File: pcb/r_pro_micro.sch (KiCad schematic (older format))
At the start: 27 parts, among them J1 Conn_01x12, J2 USB_A, J3 Conn_01x12, U1 MIC5219-2.5YM5, U2 ATmega32U4-MU, Y1 16MHz

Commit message: ** Se agregan footprints **
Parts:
- C1, C2: footprint (none) -> Capacitor_Tantalum_SMD:CP_EIA-3216-10_Kemet-I
- C3, C4, C5, C6, C7, C8, C9: footprint (none) -> Capacitor_SMD:C_0201_0603Metric
- D1: footprint (none) -> Diode_SMD:D_SOD-323
- D2, D3, D4: footprint (none) -> LED_SMD:LED_0201_0603Metric
- F1: footprint (none) -> Fuse:Fuse_1206_3216Metric
- J1, J3: footprint (none) -> Connector_PinHeader_2.54mm:PinHeader_1x12_P2.54mm_Vertical
- J2: footprint (none) -> Connector_USB:USB_Micro-AB_Molex_47590-0001; symbol Connector:USB_A -> r_pro_micro-rescue:USB_A-Connector
- R1, R2, R3, R4, R5, R6, R7: footprint (none) -> Resistor_SMD:R_0603_1608Metric
- Y1: footprint (none) -> Crystal:Crystal_SMD_5032-4Pin_5.0x3.2mm
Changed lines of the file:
@@
 F 0 "C6" H 7200 3050 50  0000 C CNN
 F 1 "22pF" H 7250 2850 50  0000 C CNN
-F 2 "" H 7150 2950 50  0001 C CNN
+F 2 "Capacitor_SMD:C_0201_0603Metric" H 7150 2950 50  0001 C CNN
 F 3 "~" H 7150 2950 50  0001 C CNN
 	1    7150 2950
@@
 F 0 "C5" H 7500 3050 50  0000 C CNN
 F 1 "22pF" H 7500 2850 50  0000 C CNN
-F 2 "" H 7600 2950 50  0001 C CNN
+F 2 "Capacitor_SMD:C_0201_0603Metric" H 7600 2950 50  0001 C CNN
 F 3 "~" H 7600 2950 50  0001 C CNN
 	1    7600 2950
@@
 F 0 "Y1" H 7350 2400 50  0000 L CNN
 F 1 "16MHz" H 7300 2600 50  0000 L CNN
-F 2 "" H 7400 2500 50  0001 C CNN
+F 2 "Crystal:Crystal_SMD_5032-4Pin_5.0x3.2mm" H 7400 2500 50  0001 C CNN
 F 3 "~" H 7400 2500 50  0001 C CNN
 	1    7400 2500
@@
 F 0 "R4" H 8100 1950 50  0000 L CNN
 F 1 "10K" H 8050 1850 50  0000 L CNN
-F 2 "" H 8250 1900 50  0001 C CNN
+F 2 "Resistor_SMD:R_0603_1608Metric" H 8250 1900 50  0001 C CNN
 F 3 "~" H 8250 1900 50  0001 C CNN
 	1    8250 1900
@@
 F 0 "C7" V 8200 2600 50  0000 C CNN
 F 1 "0.1uF" V 8300 2550 50  0000 C CNN
-F 2 "" H 8250 2700 50  0001 C CNN
+F 2 "Capacitor_SMD:C_0201_0603Metric" H 8250 2700 50  0001 C CNN
 F 3 "~" H 8250 2700 50  0001 C CNN
 	1    8250 2700
@@
 F 0 "C8" V 8150 3300 50  0000 C CNN
 F 1 "1uF" V 8250 3250 50  0000 C CNN
-F 2 "" H 8200 3400 50  0001 C CNN
+F 2 "Capacitor_SMD:C_0201_0603Metric" H 8200 3400 50  0001 C CNN
 F 3 "~" H 8200 3400 50  0001 C CNN
 	1    8200 3400
@@
 F 0 "D4" V 10654 3148 50  0000 L CNN
 F 1 "Green" V 10745 3148 50  0000 L CNN
-F 2 "" V 10700 3050 50  0001 C CNN
+F 2 "LED_SMD:LED_0201_0603Metric" V 10700 3050 50  0001 C CNN
 F 3 "~" V 10700 3050 50  0001 C CNN
 	1    10700 3050
@@
 F 0 "R6" H 10759 3596 50  0000 L CNN
 F 1 "330" H 10759 3505 50  0000 L CNN
-F 2 "" H 10700 3550 50  0001 C CNN
+F 2 "Resistor_SMD:R_0603_1608Metric" H 10700 3550 50  0001 C CNN
 F 3 "~" H 10700 3550 50  0001 C CNN
 	1    10700 3550
@@
 F 0 "R5" H 10759 1796 50  0000 L CNN
 F 1 "330" H 10759 1705 50  0000 L CNN
-F 2 "" H 10700 1750 50  0001 C CNN
+F 2 "Resistor_SMD:R_0603_1608Metric" H 10700 1750 50  0001 C CNN
 F 3 "~" H 10700 1750 50  0001 C CNN
 	1    10700 1750
@@
 F 0 "D3" V 10654 1398 50  0000 L CNN
 F 1 "Yellow" V 10745 1398 50  0000 L CNN
-F 2 "" V 10700 1300 50  0001 C CNN
+F 2 "LED_SMD:LED_0201_0603Metric" V 10700 1300 50  0001 C CNN
 F 3 "~" V 10700 1300 50  0001 C CNN
 	1    10700 1300
@@
 Wire Notes Line
 	7000 500  7000 6150
-Text Notes 9800 950  2    100  ~ 0
+Text Notes 9800 950  2    100  ~ 20
 MICROCONTROLADOR
 $Comp
@@
 F 0 "J3" H 6450 2550 50  0000 L CNN
 F 1 "Conn_01x12" H 6300 2450 50  0000 L CNN
-F 2 "" H 6500 1800 50  0001 C CNN
+F 2 "Connector_PinHeader_2.54mm:PinHeader_1x12_P2.54mm_Vertical" H 6500 1800 50  0001 C CNN
 F 3 "~" H 6500 1800 50  0001 C CNN
 	1    6500 1800
@@
 Wire Wire Line
 	6300 2400 6050 2400
-Text Notes 5200 800  0    100  ~ 0
+Text Notes 5200 800  0    100  ~ 20
 PIN HEADERS
 Wire Notes Line
@@
 NoConn ~ 9600 4600
 $Comp
-L Connector:USB_A J2
+L r_pro_micro-rescue:USB_A-Connector J2
 U 1 1 5F660175
 P 5150 4400
 F 0 "J2" H 5207 4867 50  0000 C CNN
 F 1 "USB_A" H 5207 4776 50  0000 C CNN
-F 2 "" H 5300 4350 50  0001 C CNN
+F 2 "Connector_USB:USB_Micro-AB_Molex_47590-0001" H 5300 4350 50  0001 C CNN
 F 3 " ~" H 5300 4350 50  0001 C CNN
 	1    5150 4400
@@
 F 0 "R2" V 5650 4300 50  0000 C CNN
 F 1 "22" V 5650 4500 50  0000 C CNN
-F 2 "" H 5750 4400 50  0001 C CNN
+F 2 "Resistor_SMD:R_0603_1608Metric" H 5750 4400 50  0001 C CNN
 F 3 "~" H 5750 4400 50  0001 C CNN
 	1    5750 4400
@@
 F 0 "R3" V 5850 4400 50  0000 C CNN
 F 1 "22" V 5850 4600 50  0000 C CNN
-F 2 "" H 5750 4500 50  0001 C CNN
+F 2 "Resistor_SMD:R_0603_1608Metric" H 5750 4500 50  0001 C CNN
 F 3 "~" H 5750 4500 50  0001 C CNN
 	1    5750 4500
@@
 Wire Notes Line
 	4350 6150 11200 6150
-Text Notes 5500 3250 0    100  ~ 0
+Text Notes 5500 3250 0    100  ~ 20
 USB
 Wire Notes Line
@@
 F 0 "J1" H 4718 1075 50  0000 C CNN
 F 1 "Conn_01x12" H 4718 1166 50  0000 C CNN
-F 2 "" H 4800 1900 50  0001 C CNN
+F 2 "Connector_PinHeader_2.54mm:PinHeader_1x12_P2.54mm_Vertical" H 4800 1900 50  0001 C CNN
 F 3 "~" H 4800 1900 50  0001 C CNN
 	1    4800 1900
@@
 F 0 "C1" H 1741 2646 50  0000 L CNN
 F 1 "10uF" H 1741 2555 50  0000 L CNN
-F 2 "" H 1650 2600 50  0001 C CNN
+F 2 "Capacitor_Tantalum_SMD:CP_EIA-3216-10_Kemet-I" H 1650 2600 50  0001 C CNN
 F 3 "~" H 1650 2600 50  0001 C CNN
 	1    1650 2600
@@
 F 0 "C2" H 2991 2646 50  0000 L CNN
 F 1 "10uF" H 2991 2555 50  0000 L CNN
-F 2 "" H 2900 2600 50  0001 C CNN
+F 2 "Capacitor_Tantalum_SMD:CP_EIA-3216-10_Kemet-I" H 2900 2600 50  0001 C CNN
 F 3 "~" H 2900 2600 50  0001 C CNN
 	1    2900 2600
@@
 F 0 "C3" H 3400 2700 50  0000 C CNN
 F 1 "1uF" H 3400 2500 50  0000 C CNN
-F 2 "" H 3300 2600 50  0001 C CNN
+F 2 "Capacitor_SMD:C_0201_0603Metric" H 3300 2600 50  0001 C CNN
 F 3 "~" H 3300 2600 50  0001 C CNN
 	1    3300 2600
@@
 F 0 "C4" H 3700 2700 50  0000 C CNN
 F 1 "1uF" H 3700 2500 50  0000 C CNN
-F 2 "" H 3600 2600 50  0001 C CNN
+F 2 "Capacitor_SMD:C_0201_0603Metric" H 3600 2600 50  0001 C CNN
 F 3 "~" H 3600 2600 50  0001 C CNN
 	1    3600 2600
@@
 F 0 "R1" H 4009 2696 50  0000 L CNN
 F 1 "1K" H 4009 2605 50  0000 L CNN
-F 2 "" H 3950 2650 50  0001 C CNN
+F 2 "Resistor_SMD:R_0603_1608Metric" H 3950 2650 50  0001 C CNN
 F 3 "~" H 3950 2650 50  0001 C CNN
 	1    3950 2650
@@
 F 0 "D2" V 3900 3000 50  0000 L CNN
 F 1 "Red" V 4000 2900 50  0000 L CNN
-F 2 "" V 3950 3200 50  0001 C CNN
+F 2 "LED_SMD:LED_0201_0603Metric" V 3950 3200 50  0001 C CNN
 F 3 "~" V 3950 3200 50  0001 C CNN
 	1    3950 3200
@@
 F 0 "F1" V 795 2000 50  0000 C CNN
 F 1 "500mA" V 886 2000 50  0000 C CNN
-F 2 "" H 1050 1800 50  0001 L CNN
+F 2 "Fuse:Fuse_1206_3216Metric" H 1050 1800 50  0001 L CNN
 F 3 "~" H 1000 2000 50  0001 C CNN
 	1    1000 2000
@@
 F 0 "D1" H 1450 1793 50  0000 C CNN
 F 1 "D" H 1450 1884 50  0000 C CNN
-F 2 "" V 1450 2000 50  0001 C CNN
+F 2 "Diode_SMD:D_SOD-323" V 1450 2000 50  0001 C CNN
 F 3 "~" V 1450 2000 50  0001 C CNN
 	1    1450 2000
@@
 Wire Wire Line
 	1650 2000 1650 2350
-Text Notes 2000 1450 0    100  ~ 0
+Text Notes 2000 1450 0    100  ~ 20
 REGULADOR
 Wire Wire Line
@@
 F 0 "C9" H 2300 4250 50  0000 C CNN
 F 1 "1uF" H 2300 4050 50  0000 C CNN
-F 2 "" H 2200 4150 50  0001 C CNN
+F 2 "Capacitor_SMD:C_0201_0603Metric" H 2200 4150 50  0001 C CNN
 F 3 "~" H 2200 4150 50  0001 C CNN
 	1    2200 4150
@@
 F 0 "R7" V 10200 4150 50  0000 L CNN
 F 1 "0" V 10400 4150 50  0000 L CNN
-F 2 "" H 10300 4200 50  0001 C CNN
+F 2 "Resistor_SMD:R_0603_1608Metric" H 10300 4200 50  0001 C CNN
 F 3 "~" H 10300 4200 50  0001 C CNN
 	1    10300 4200

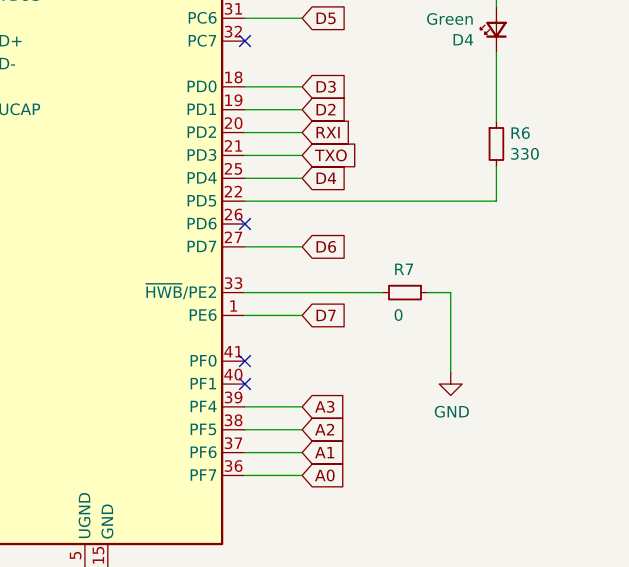
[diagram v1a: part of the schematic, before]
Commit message: ** Se crea netlist cambiando R 0omhs por nettie **
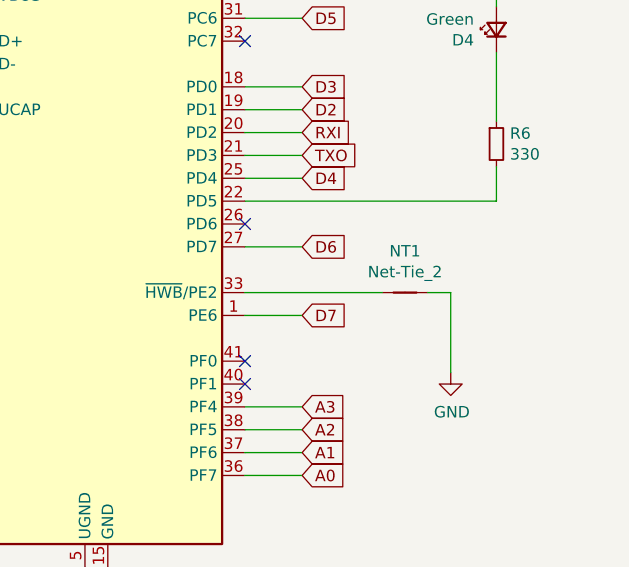
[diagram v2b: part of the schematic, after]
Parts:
- removed R7: 0, Resistor_SMD:R_0603_1608Metric, symbol Device:R_Small
- added NT1: Net-Tie_2, NetTie:NetTie-2_SMD_Pad0.5mm, symbol Device:Net-Tie_2
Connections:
- net GND: now also NT1.2
- net at U2.33 (~HWB~/PE2): now also NT1.1
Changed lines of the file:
@@
 Wire Wire Line
 	1650 2800 1650 2850
-$Comp
-L Device:R_Small R7
-U 1 1 5F6CBCA3
-P 10300 4200
-F 0 "R7" V 10200 4150 50  0000 L CNN
-F 1 "0" V 10400 4150 50  0000 L CNN
-F 2 "Resistor_SMD:R_0603_1608Metric" H 10300 4200 50  0001 C CNN
-F 3 "~" H 10300 4200 50  0001 C CNN
-	1    10300 4200
-	0    1    1    0
-$EndComp
 Wire Wire Line
 	10200 4200 9600 4200
@@
 	1    0    0    -1
 $EndComp
+$Comp
+L Device:Net-Tie_2 NT1
+U 1 1 5F7FD2D5
+P 10300 4200
+F 0 "NT1" H 10300 4381 50  0000 C CNN
+F 1 "Net-Tie_2" H 10300 4290 50  0000 C CNN
+F 2 "NetTie:NetTie-2_SMD_Pad0.5mm" H 10300 4200 50  0001 C CNN
+F 3 "~" H 10300 4200 50  0001 C CNN
+	1    10300 4200
+	1    0    0    -1
+$EndComp

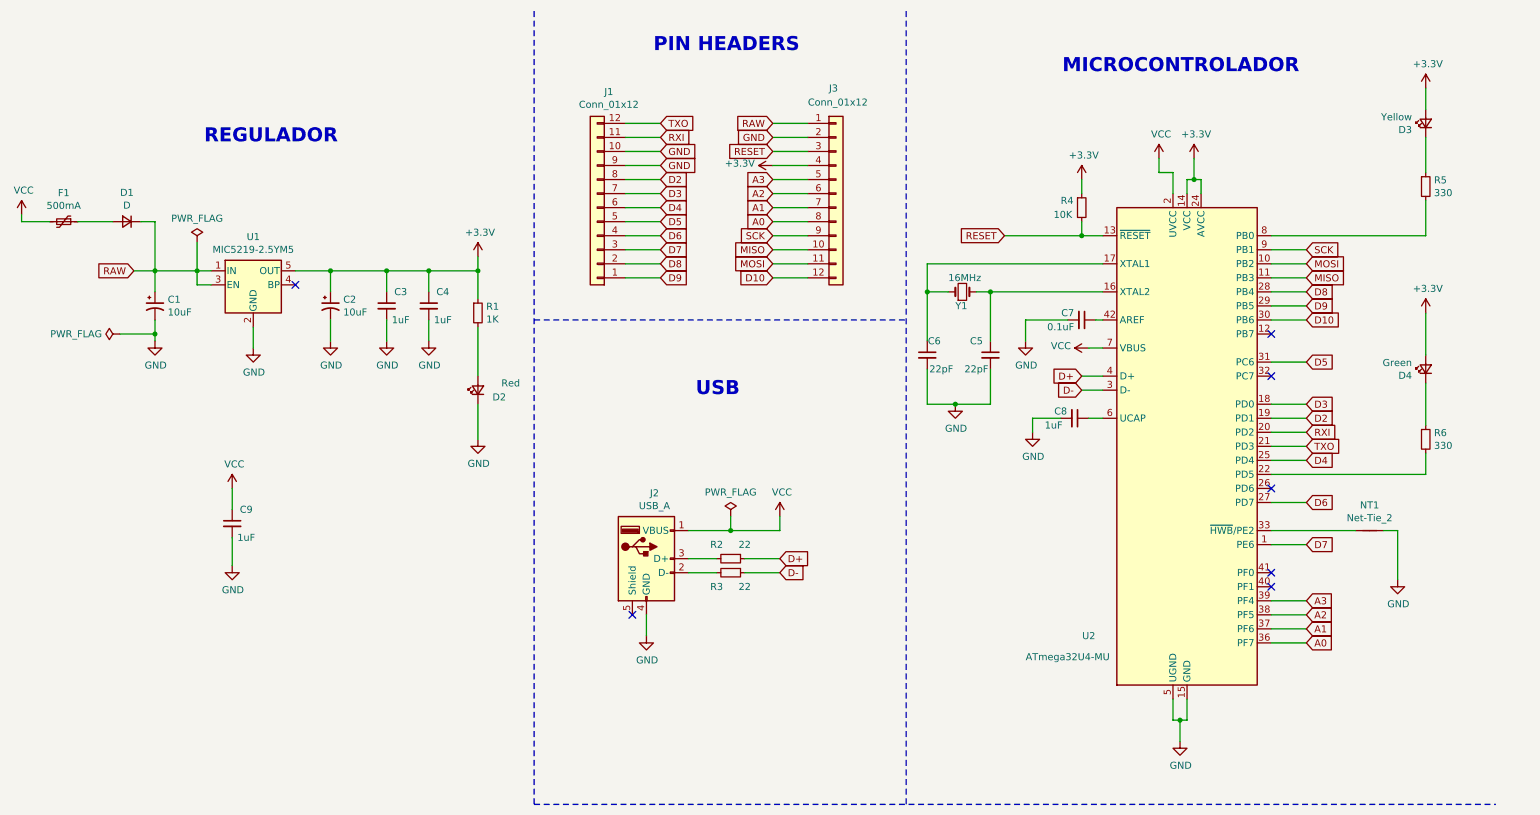
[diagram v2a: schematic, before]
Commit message: ** Se modifica etiquetas y disposicion del esquematico **
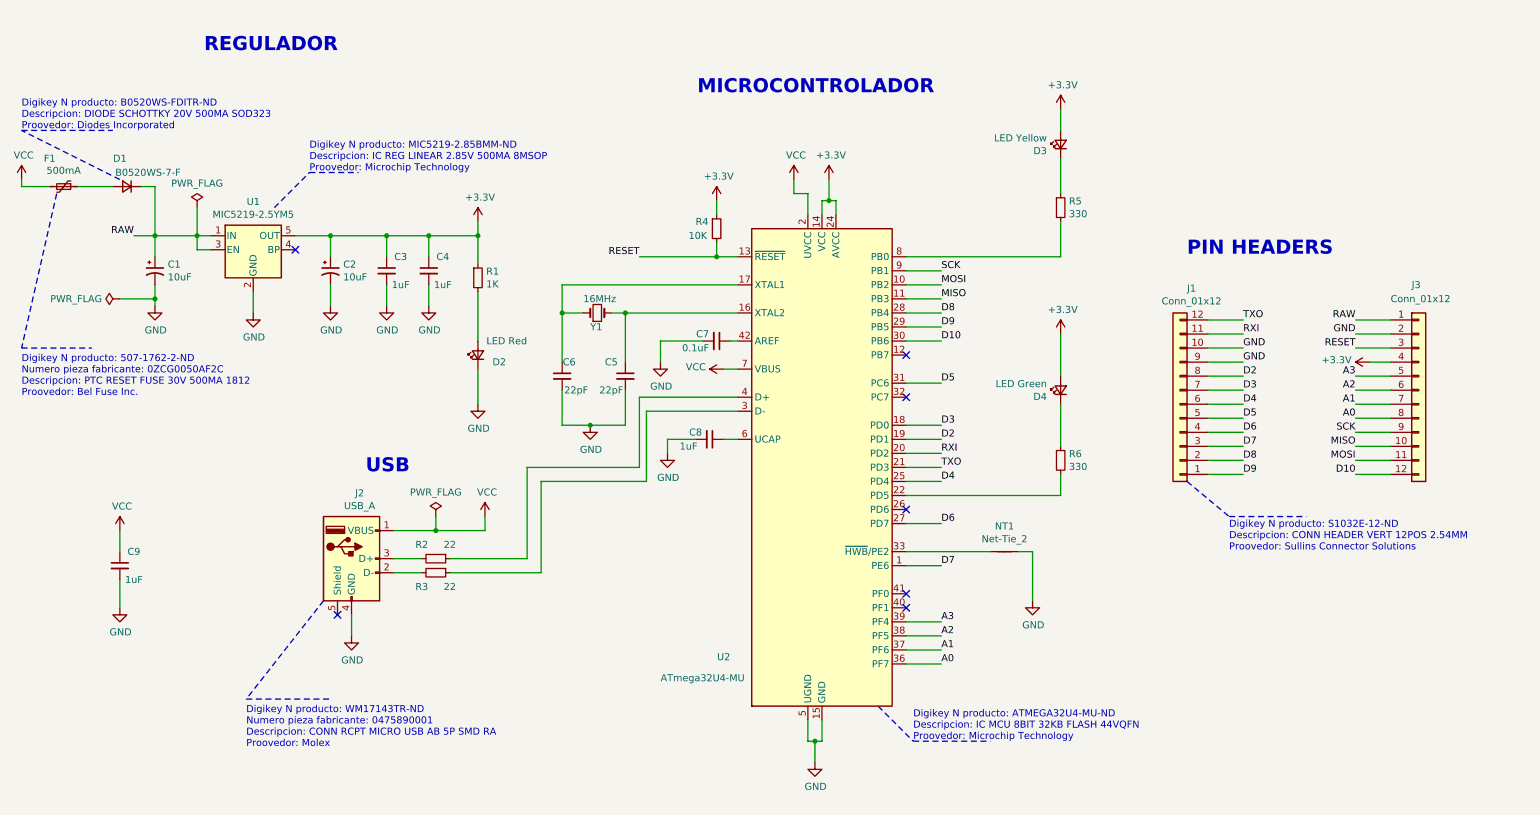
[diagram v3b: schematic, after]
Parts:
- D1: value D -> B0520WS-7-F
- D2: value Red -> LED Red
- D3: value Yellow -> LED Yellow
- D4: value Green -> LED Green
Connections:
- net D+: no longer names the net of R2.1, U2.4 (D+)
- net D-: no longer names the net of R3.1, U2.3 (D-)
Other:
- note added: "Digikey N producto: 507-1762-2-ND\nNumero pieza fabricante: 0ZCG0050AF2C\nDescripcion: PTC RESET FUSE 30V 500MA 1812\nProovedor: Bel Fuse Inc."
- note added: "Digikey N producto: ATMEGA32U4-MU-ND\nDescripcion: IC MCU 8BIT 32KB FLASH 44VQFN\nProovedor: Microchip Technology"
- note added: "Digikey N producto: B0520WS-FDITR-ND\nDescripcion: DIODE SCHOTTKY 20V 500MA SOD323\nProovedor: Diodes Incorporated"
- note added: "Digikey N producto: MIC5219-2.85BMM-ND\nDescripcion: IC REG LINEAR 2.85V 500MA 8MSOP\nProovedor: Microchip Technology"
- note added: "Digikey N producto: S1032E-12-ND\nDescripcion: CONN HEADER VERT 12POS 2.54MM\nProovedor: Sullins Connector Solutions"
- note added: "Digikey N producto: WM17143TR-ND\nNumero pieza fabricante: 0475890001\nDescripcion: CONN RCPT MICRO USB AB 5P SMD RA\nProovedor: Molex"
- moved on the sheet: C1, C2, C3, C4, C5, C6, C7, C8, C9, D1, D2, D3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

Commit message: ** Se cambian huellas a 0805 **
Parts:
- C3, C4, C5, C6, C7, C8, C9: footprint Capacitor_SMD:C_0201_0603Metric -> Capacitor_SMD:C_0805_2012Metric
- D2, D3, D4: footprint LED_SMD:LED_0201_0603Metric -> LED_SMD:LED_0805_2012Metric
- R1, R2, R3, R4, R5, R6: footprint Resistor_SMD:R_0603_1608Metric -> Resistor_SMD:R_0805_2012Metric
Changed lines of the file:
@@
 F 0 "R6" H 8159 3746 50  0000 L CNN
 F 1 "330" H 8159 3655 50  0000 L CNN
-F 2 "Resistor_SMD:R_0603_1608Metric" H 8100 3700 50  0001 C CNN
+F 2 "Resistor_SMD:R_0805_2012Metric" H 8100 3700 50  0001 C CNN
 F 3 "~" H 8100 3700 50  0001 C CNN
 	1    8100 3700
@@
 F 0 "R5" H 8159 1946 50  0000 L CNN
 F 1 "330" H 8159 1855 50  0000 L CNN
-F 2 "Resistor_SMD:R_0603_1608Metric" H 8100 1900 50  0001 C CNN
+F 2 "Resistor_SMD:R_0805_2012Metric" H 8100 1900 50  0001 C CNN
 F 3 "~" H 8100 1900 50  0001 C CNN
 	1    8100 1900
@@
 F 0 "R2" V 3550 4300 50  0000 C CNN
 F 1 "22" V 3550 4500 50  0000 C CNN
-F 2 "Resistor_SMD:R_0603_1608Metric" H 3650 4400 50  0001 C CNN
+F 2 "Resistor_SMD:R_0805_2012Metric" H 3650 4400 50  0001 C CNN
 F 3 "~" H 3650 4400 50  0001 C CNN
 	1    3650 4400
@@
 F 0 "R3" V 3750 4400 50  0000 C CNN
 F 1 "22" V 3750 4600 50  0000 C CNN
-F 2 "Resistor_SMD:R_0603_1608Metric" H 3650 4500 50  0001 C CNN
+F 2 "Resistor_SMD:R_0805_2012Metric" H 3650 4500 50  0001 C CNN
 F 3 "~" H 3650 4500 50  0001 C CNN
 	1    3650 4500
@@
 F 0 "C9" H 1500 4550 50  0000 C CNN
 F 1 "1uF" H 1500 4350 50  0000 C CNN
-F 2 "Capacitor_SMD:C_0201_0603Metric" H 1400 4450 50  0001 C CNN
+F 2 "Capacitor_SMD:C_0805_2012Metric" H 1400 4450 50  0001 C CNN
 F 3 "~" H 1400 4450 50  0001 C CNN
 	1    1400 4450
@@
 F 0 "D3" V 8054 1548 50  0000 L CNN
 F 1 "LED Yellow" V 8145 1548 50  0000 L CNN
-F 2 "LED_SMD:LED_0201_0603Metric" V 8100 1450 50  0001 C CNN
+F 2 "LED_SMD:LED_0805_2012Metric" V 8100 1450 50  0001 C CNN
 F 3 "~" V 8100 1450 50  0001 C CNN
 	1    8100 1450
@@
 F 0 "D4" V 8054 3298 50  0000 L CNN
 F 1 "LED Green" V 8145 3298 50  0000 L CNN
-F 2 "LED_SMD:LED_0201_0603Metric" V 8100 3200 50  0001 C CNN
+F 2 "LED_SMD:LED_0805_2012Metric" V 8100 3200 50  0001 C CNN
 F 3 "~" V 8100 3200 50  0001 C CNN
 	1    8100 3200
@@
 F 0 "C8" V 5550 3450 50  0000 C CNN
 F 1 "1uF" V 5650 3400 50  0000 C CNN
-F 2 "Capacitor_SMD:C_0201_0603Metric" H 5600 3550 50  0001 C CNN
+F 2 "Capacitor_SMD:C_0805_2012Metric" H 5600 3550 50  0001 C CNN
 F 3 "~" H 5600 3550 50  0001 C CNN
 	1    5600 3550
@@
 F 0 "C7" V 5600 2750 50  0000 C CNN
 F 1 "0.1uF" V 5700 2700 50  0000 C CNN
-F 2 "Capacitor_SMD:C_0201_0603Metric" H 5650 2850 50  0001 C CNN
+F 2 "Capacitor_SMD:C_0805_2012Metric" H 5650 2850 50  0001 C CNN
 F 3 "~" H 5650 2850 50  0001 C CNN
 	1    5650 2850
@@
 F 0 "R4" H 5500 2100 50  0000 L CNN
 F 1 "10K" H 5450 2000 50  0000 L CNN
-F 2 "Resistor_SMD:R_0603_1608Metric" H 5650 2050 50  0001 C CNN
+F 2 "Resistor_SMD:R_0805_2012Metric" H 5650 2050 50  0001 C CNN
 F 3 "~" H 5650 2050 50  0001 C CNN
 	1    5650 2050
@@
 F 0 "C5" H 4900 3200 50  0000 C CNN
 F 1 "22pF" H 4900 3000 50  0000 C CNN
-F 2 "Capacitor_SMD:C_0201_0603Metric" H 5000 3100 50  0001 C CNN
+F 2 "Capacitor_SMD:C_0805_2012Metric" H 5000 3100 50  0001 C CNN
 F 3 "~" H 5000 3100 50  0001 C CNN
 	1    5000 3100
@@
 F 0 "C6" H 4600 3200 50  0000 C CNN
 F 1 "22pF" H 4650 3000 50  0000 C CNN
-F 2 "Capacitor_SMD:C_0201_0603Metric" H 4550 3100 50  0001 C CNN
+F 2 "Capacitor_SMD:C_0805_2012Metric" H 4550 3100 50  0001 C CNN
 F 3 "~" H 4550 3100 50  0001 C CNN
 	1    4550 3100
@@
 F 0 "D2" V 3900 2750 50  0000 L CNN
 F 1 "LED Red" V 4050 2600 50  0000 L CNN
-F 2 "LED_SMD:LED_0201_0603Metric" V 3950 2950 50  0001 C CNN
+F 2 "LED_SMD:LED_0805_2012Metric" V 3950 2950 50  0001 C CNN
 F 3 "~" V 3950 2950 50  0001 C CNN
 	1    3950 2950
@@
 F 0 "R1" H 4009 2446 50  0000 L CNN
 F 1 "1K" H 4009 2355 50  0000 L CNN
-F 2 "Resistor_SMD:R_0603_1608Metric" H 3950 2400 50  0001 C CNN
+F 2 "Resistor_SMD:R_0805_2012Metric" H 3950 2400 50  0001 C CNN
 F 3 "~" H 3950 2400 50  0001 C CNN
 	1    3950 2400
@@
 F 0 "C4" H 3700 2450 50  0000 C CNN
 F 1 "1uF" H 3700 2250 50  0000 C CNN
-F 2 "Capacitor_SMD:C_0201_0603Metric" H 3600 2350 50  0001 C CNN
+F 2 "Capacitor_SMD:C_0805_2012Metric" H 3600 2350 50  0001 C CNN
 F 3 "~" H 3600 2350 50  0001 C CNN
 	1    3600 2350
@@
 F 0 "C3" H 3400 2450 50  0000 C CNN
 F 1 "1uF" H 3400 2250 50  0000 C CNN
-F 2 "Capacitor_SMD:C_0201_0603Metric" H 3300 2350 50  0001 C CNN
+F 2 "Capacitor_SMD:C_0805_2012Metric" H 3300 2350 50  0001 C CNN
 F 3 "~" H 3300 2350 50  0001 C CNN
 	1    3300 2350
